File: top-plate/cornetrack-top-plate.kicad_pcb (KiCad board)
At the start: 2 copper layers, 133.8 x 106.7 mm, 29 parts, among them SW2 KEY_SWITCH

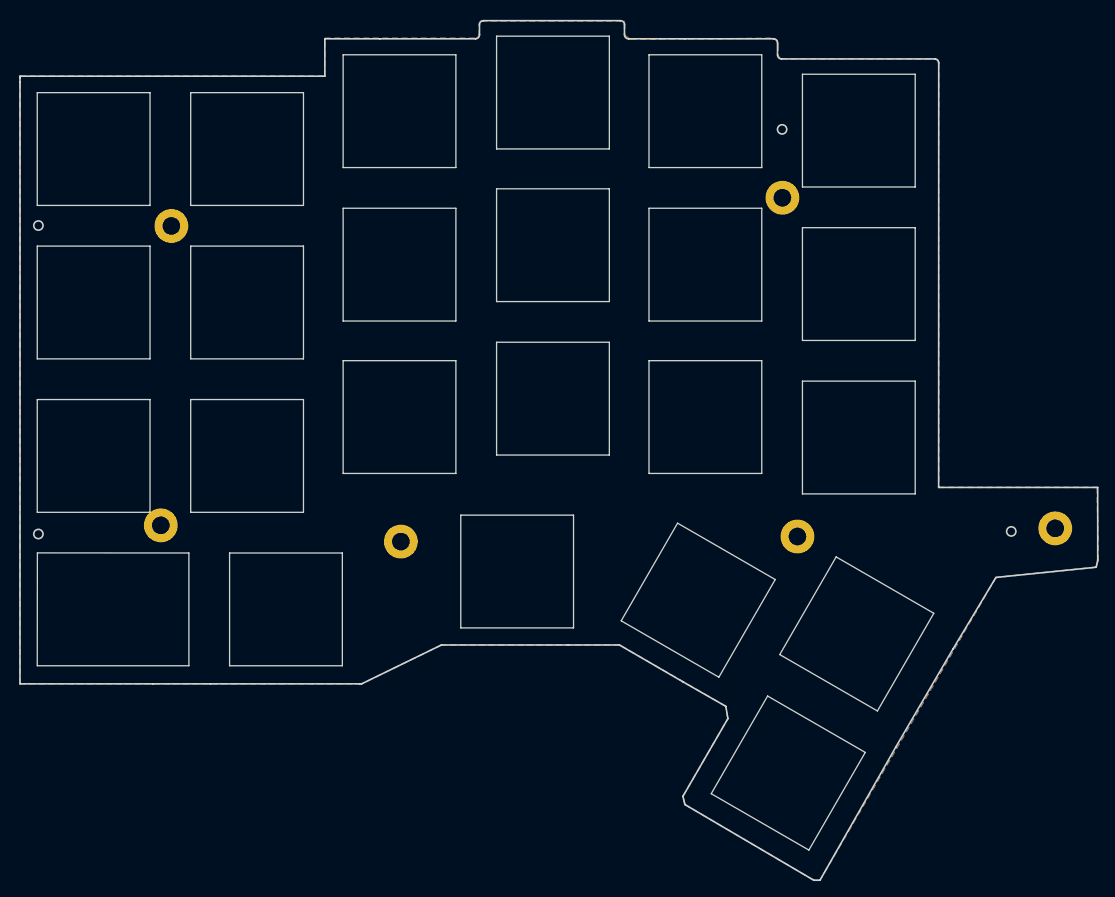
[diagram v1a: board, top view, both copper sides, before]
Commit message: made top and bottom plate a tiny bit larger in order to increase distance between edge cuts to >2mm
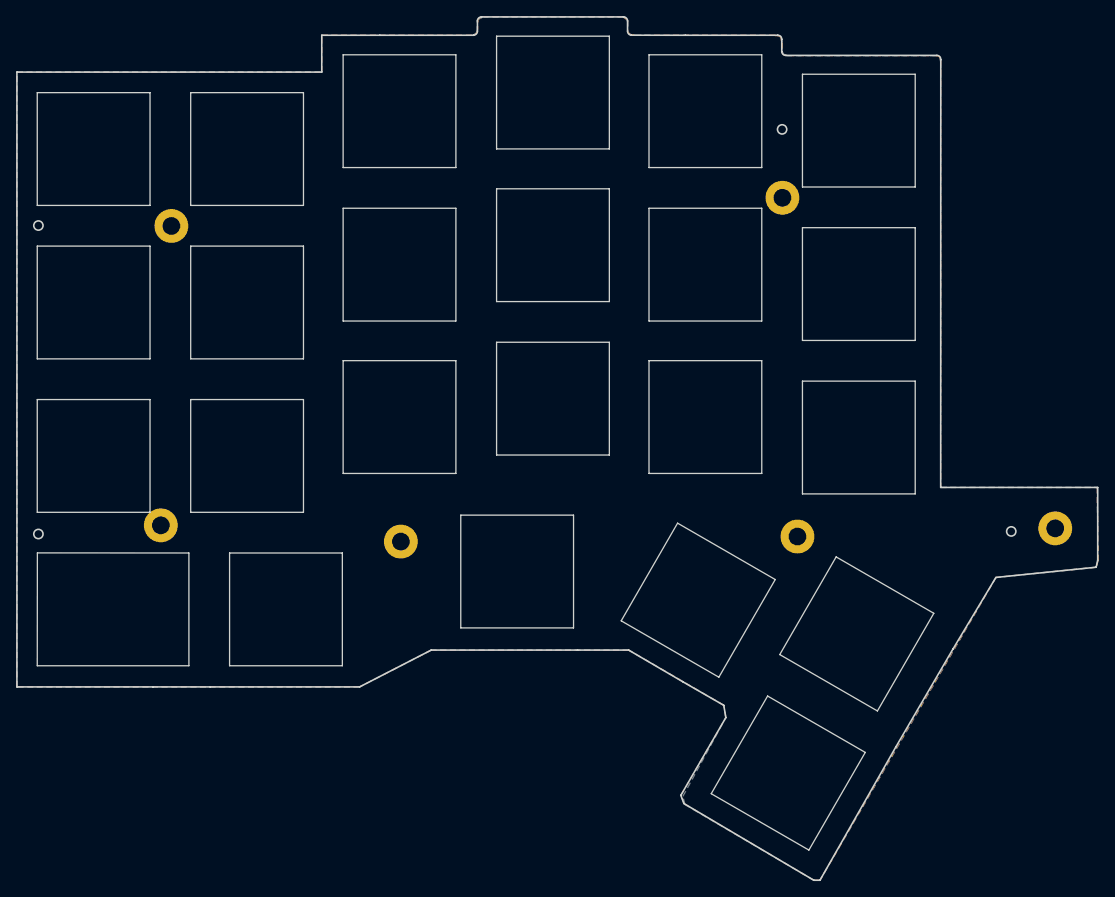
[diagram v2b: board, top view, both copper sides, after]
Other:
- board size 133.8 x 106.7 mm -> 134.2 x 107.2 mm
